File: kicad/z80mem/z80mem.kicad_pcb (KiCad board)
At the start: 2 copper layers, 6 parts, among them U1 MS628128, U2 2764, U3 z80pcb, U4 74LS32, U6 7400, U7 74LS138

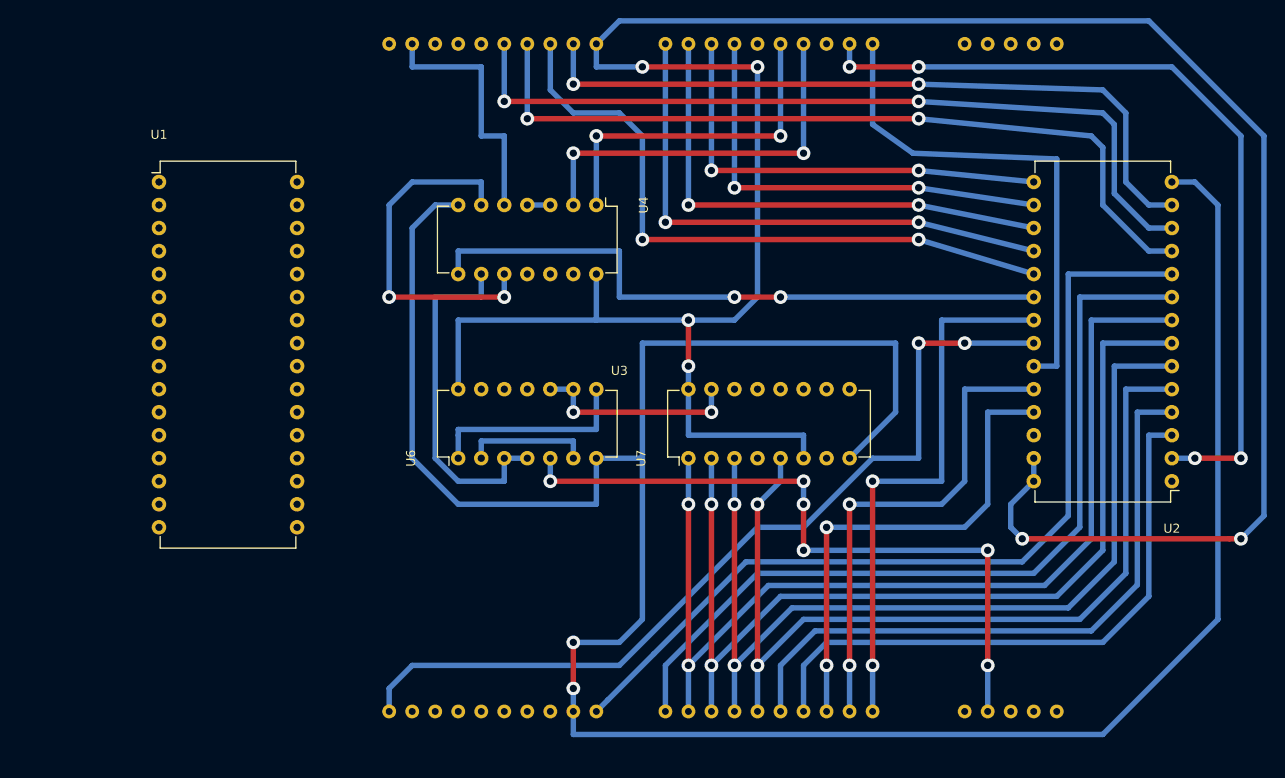
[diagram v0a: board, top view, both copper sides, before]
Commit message: add some unfished pcbs
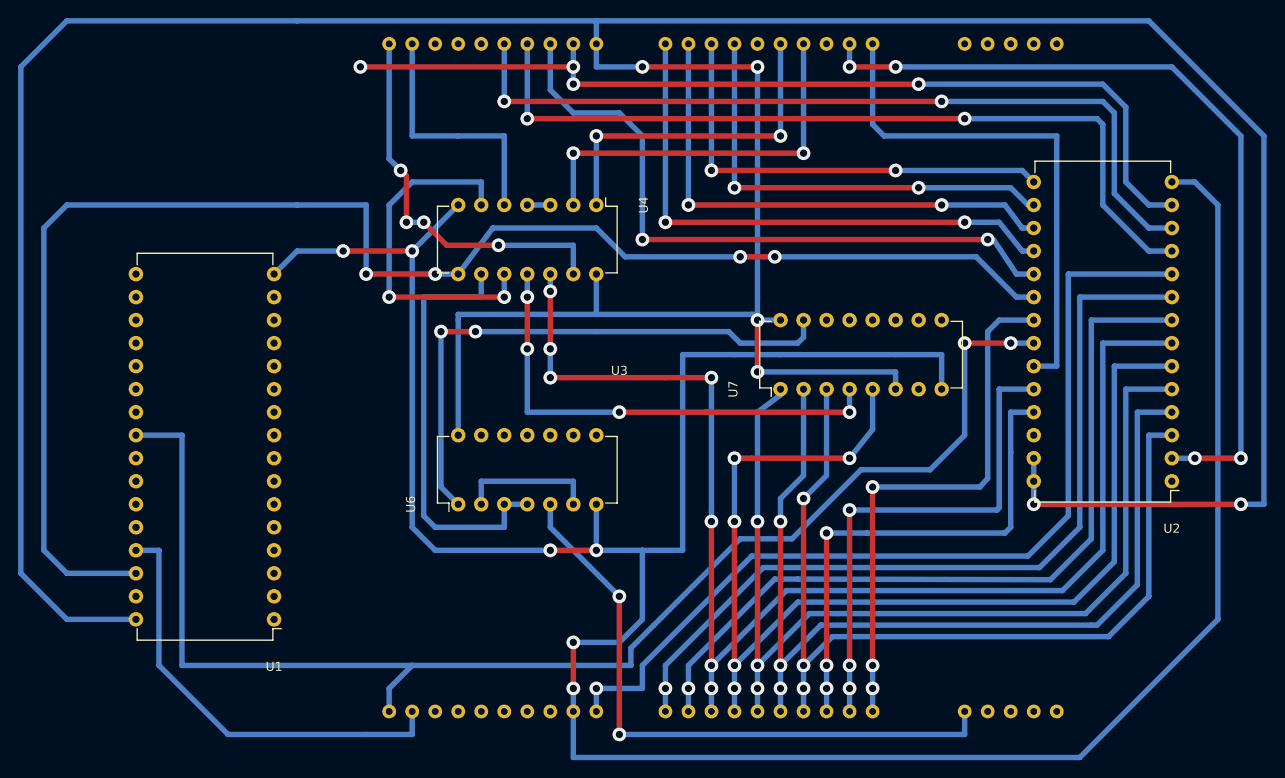
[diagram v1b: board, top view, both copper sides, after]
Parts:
- moved U1 49.9 mm to (111.8, 134.6), turned to 180 degrees
- moved U7 12.7 mm to (167.6, 109.2)
- moved U6 5.08 mm to (132.1, 121.9)
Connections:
- U1 pad 13: Net-(U1-Pad13) -> d0
- U1 pad 14: Net-(U1-Pad14) -> d3
- U1 pad 15: Net-(U1-Pad15) -> d2
- U1 pad 17: Net-(U1-Pad17) -> d1
- U1 pad 18: Net-(U1-Pad18) -> d4
- U1 pad 19: Net-(U1-Pad19) -> d5
- U1 pad 20: Net-(U1-Pad20) -> d6
- U1 pad 21: Net-(U1-Pad21) -> d7
- U3 pad 46: Net-(U3-Pad46) -> reset
- U3 pad 47: reset -> Net-(U3-Pad47)
- U4 pad 12: a6 -> a3
- U4 pad 13: a7 -> iorq
- U6 pad 10: Net-(U6-Pad10) -> (no net)
- U6 pad 8: Net-(U6-Pad1) -> (no net)
- U6 pad 9: Net-(U6-Pad10) -> (no net)
- U7 pad 1: a2 -> a5
- U7 pad 15: Net-(U6-Pad10) -> Net-(U6-Pad1)
- U7 pad 2: a3 -> a6
- U7 pad 3: a4 -> a7
- U7 pad 5: a5 -> a4
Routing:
- net VCC: track 280.5 -> 413.3 mm
- net Net-(U1-Pad30): track 71.1 -> 171.0 mm, vias 2 -> 4
- net rd: track 96.9 -> 152.4 mm
- net Net-(U4-Pad11): track 0.00 -> 54.0 mm, vias 0 -> 4
- net wr: track 0.00 -> 48.9 mm
- net iorq: track 0.00 -> 43.1 mm, vias 0 -> 4
- net Net-(U6-Pad1): track 22.9 -> 62.5 mm, vias 0 -> 2
- net a3: track 106.9 -> 145.0 mm, vias 2 -> 7
- net a6: track 71.0 -> 102.5 mm, vias 0 -> 3
- net a7: track 66.7 -> 98.2 mm, vias 0 -> 3
- net d2: track 80.2 -> 104.3 mm, vias 2 -> 4
- net Net-(U6-Pad10): track 22.9 -> 0.00 mm, vias 2 -> 0
- net a2: track 111.2 -> 89.0 mm, vias 2 -> 1
- net a4: track 102.5 -> 123.7 mm, vias 2 -> 5
- net GND: track 284.4 -> 302.2 mm, vias 2 -> 6
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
